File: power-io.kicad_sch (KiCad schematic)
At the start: 30 parts, among them J1 USB4105-GF-A, J2 J2 GPIO / 2.00mm, J3 J3 GPIO / 2.00mm, SW1 RESET, SW2 BOOT, U2 AP2112K-3.3, U4 SN74LV1T125

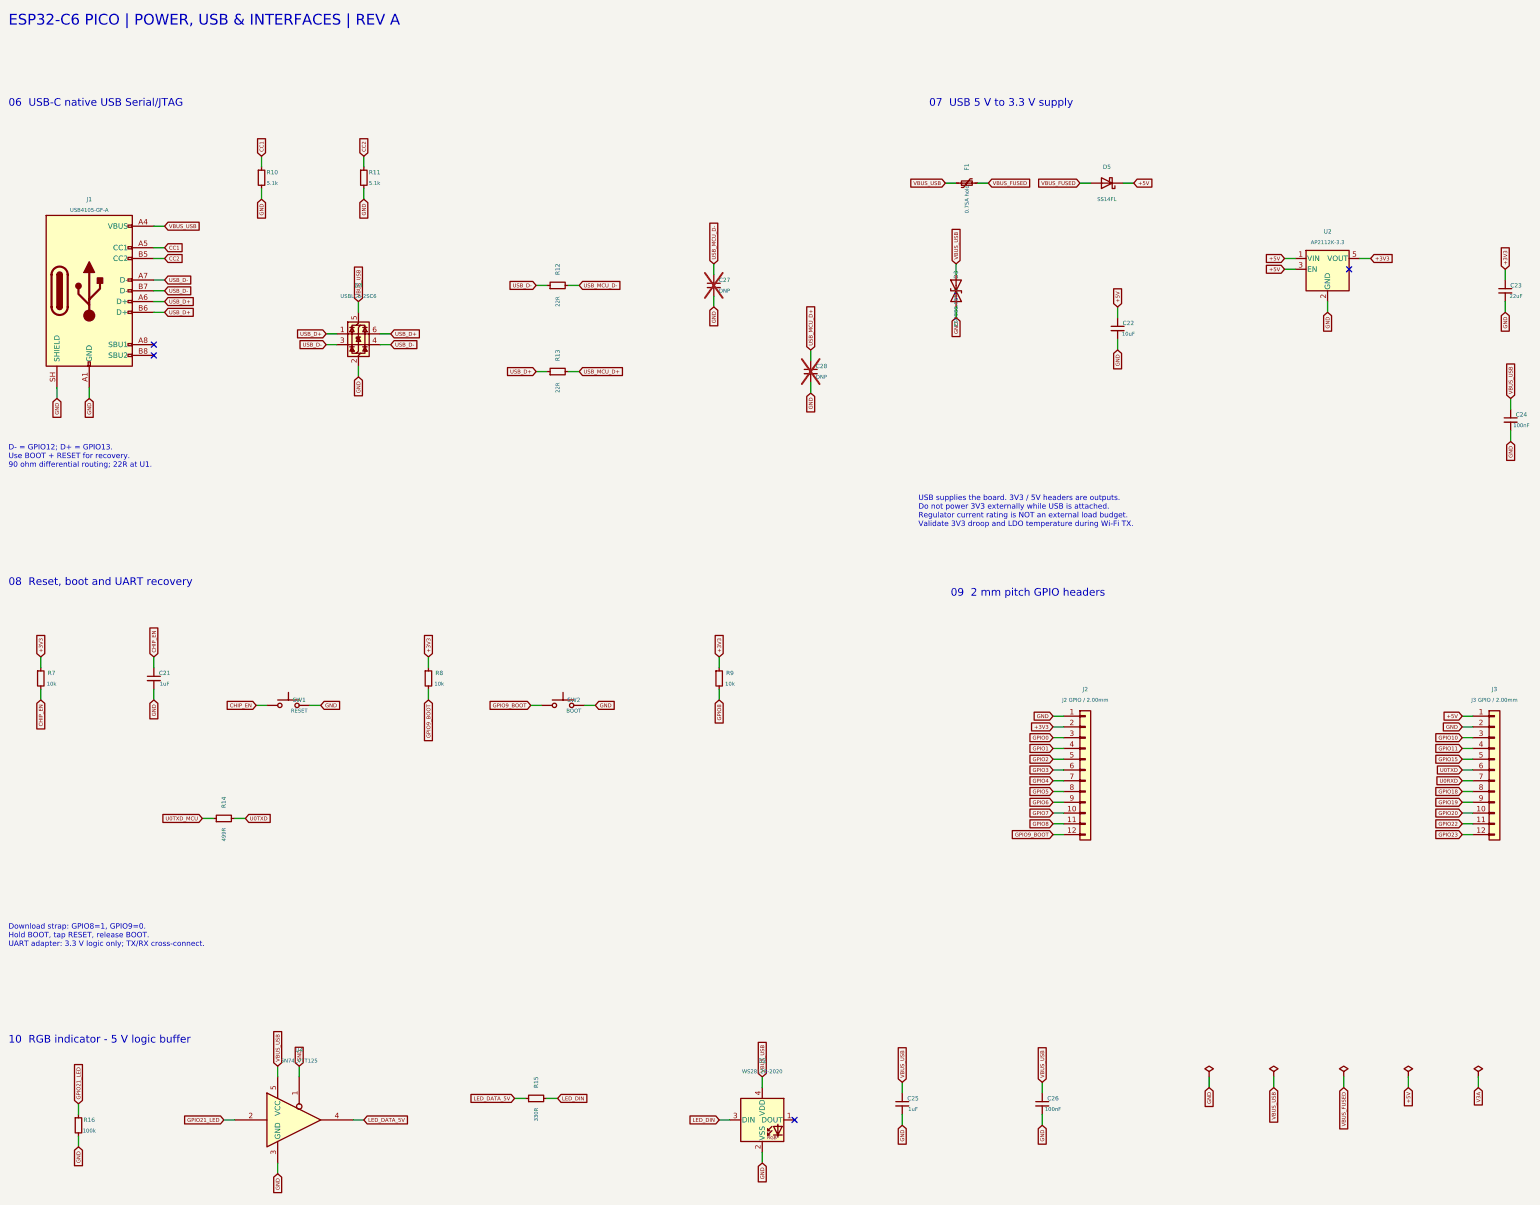
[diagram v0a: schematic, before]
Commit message: Refine ESP32-C6 Pico layout and project handoff
Update the 20.5 x 32 mm layout, antenna and crystal placement, USB routing, via clearances, and silkscreen logos. Keep RF passives at 0201 and use 0402 for all other resistors and capacitors. Draw ESP32-C6 peripherals directly from U1 pins.

Refresh BOM, placement files, previews, validation reports, and project guidance. Exclude KiCad backup folders, autosaves, and local state on Windows and Linux.

Validation: ERC, DRC, and unconnected counts are zero; all 45 QA checks passed. Verify final file hashes and backup exclusions before commit.
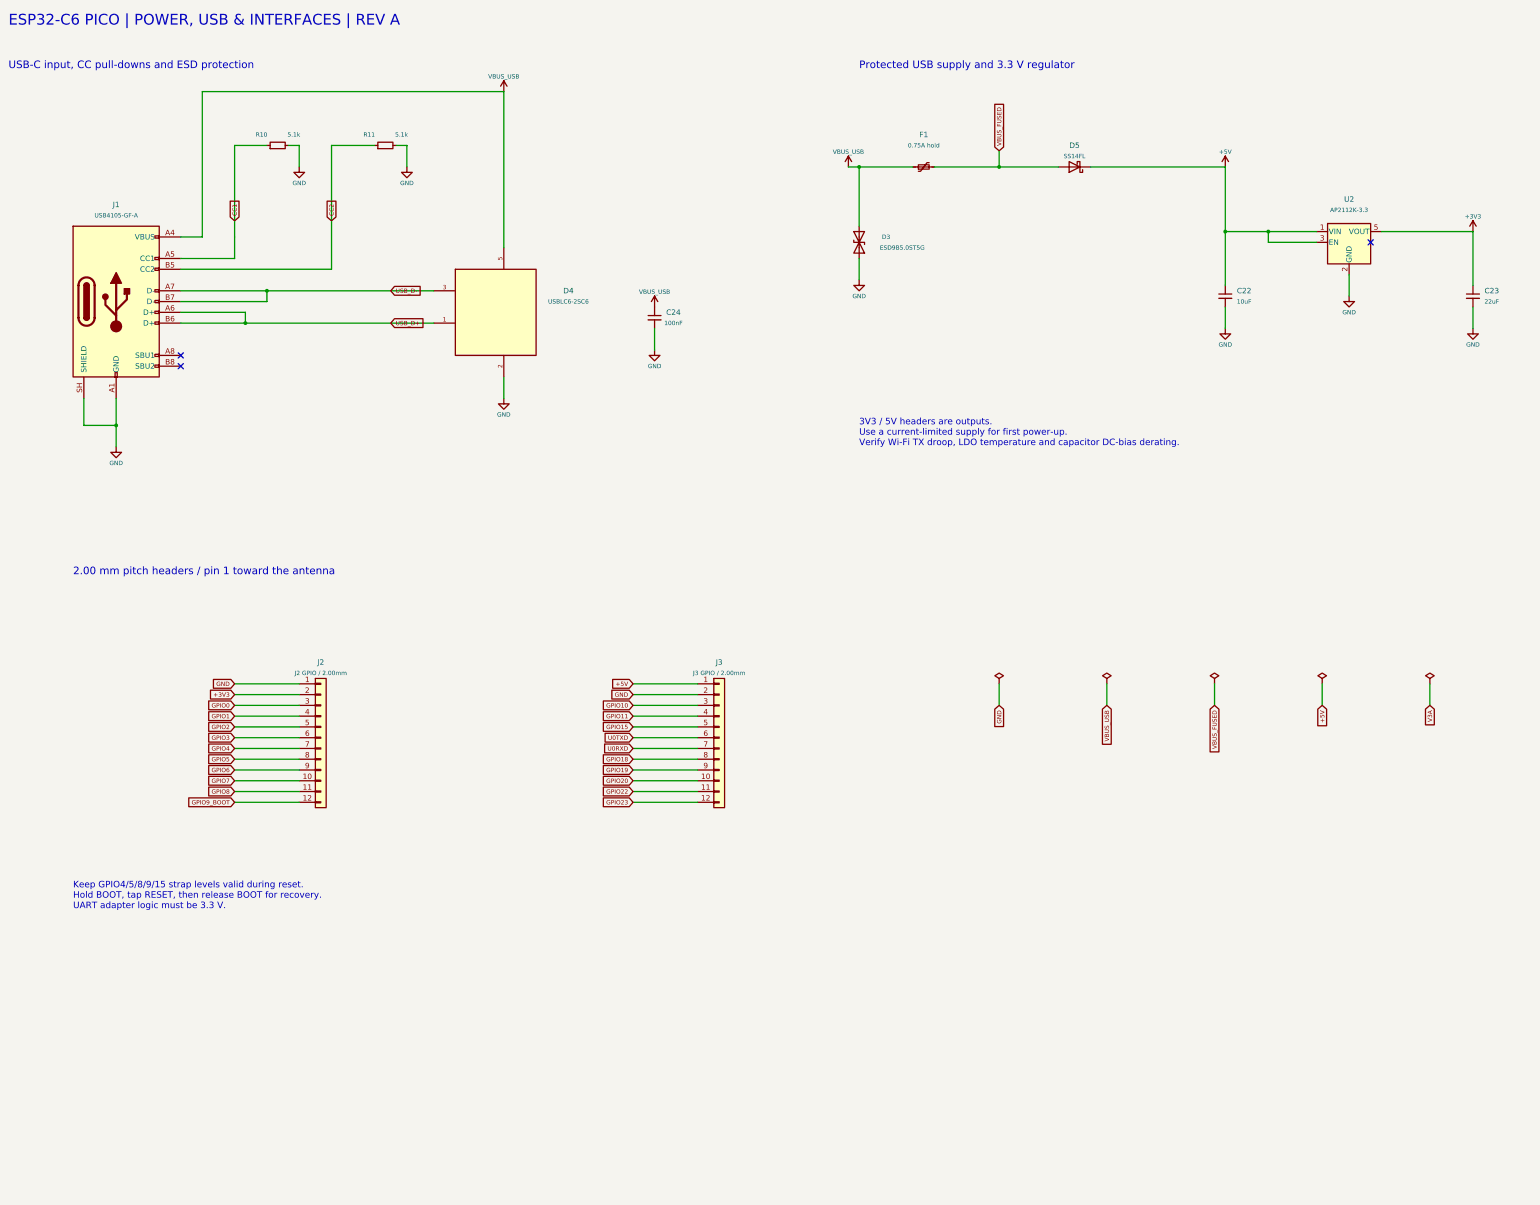
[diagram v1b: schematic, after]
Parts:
- removed C21, C25: 1uF, Capacitor_SMD:C_0402_1005Metric, symbol Pico_Design:Device__C_Small
- removed C26: 100nF, Capacitor_SMD:C_0402_1005Metric, symbol Pico_Design:Device__C_Small
- removed C27, C28: DNP, Capacitor_SMD:C_0402_1005Metric, symbol Pico_Design:Device__C_Small
- removed D2: WS2812B-2020, Pico:WS2812B_2020_Compact, symbol Pico_Design:LED__WS2812B-2020
- removed R12, R13: 22R, Resistor_SMD:R_0402_1005Metric, symbol Pico_Design:Device__R_Small
- removed R14: 499R, Resistor_SMD:R_0402_1005Metric, symbol Pico_Design:Device__R_Small
- removed R15: 330R, Resistor_SMD:R_0402_1005Metric, symbol Pico_Design:Device__R_Small
- removed R16: 100k, Resistor_SMD:R_0402_1005Metric, symbol Pico_Design:Device__R_Small
- removed R7, R8, R9: 10k, Resistor_SMD:R_0402_1005Metric, symbol Pico_Design:Device__R_Small
- removed SW1: RESET, Button_Switch_SMD:SW_Push_1P1T_NO_CK_KMR2, symbol Pico_Design:Switch__SW_Push
- removed SW2: BOOT, Button_Switch_SMD:SW_Push_1P1T_NO_CK_KMR2, symbol Pico_Design:Switch__SW_Push
- removed U4: SN74LV1T125, Package_TO_SOT_SMD:SOT-23-5, symbol Pico_Design:Pico_Custom__SN74LV1T125
- C22: footprint Capacitor_SMD:C_0603_1608Metric -> Capacitor_SMD:C_0402_1005Metric; AssemblyNote 10 V X7R; regulator input -> Regulator input; 0402, 10 V minimum; X5R reference; verify 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
- C23: footprint Capacitor_SMD:C_0603_1608Metric -> Capacitor_SMD:C_0402_1005Metric; AssemblyNote 10 V X5R/X7R; verify DC-bias effective capacitance -> Regulator output; 0402, 22 uF nominal, 10 V minimum; X5R re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
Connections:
- no-connect marks 4 -> 3
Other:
- note added: "2.00 mm pitch headers / pin 1 toward the antenna"
- note added: "3V3 / 5V headers are outputs. Use a current-limited supply for first power-up. Verify Wi-Fi TX droop, LDO temperature and capacitor DC-bias derating."
- note added: "Keep GPIO4/5/8/9/15 strap levels valid during reset. Hold BOOT, tap RESET, then release BOOT for recovery. UART adapter logic must be 3.3 V."
- note added: "Protected USB supply and 3.3 V regulator"
- note added: "USB-C input, CC pull-downs and ESD protection"
- note removed: "06 USB-C native USB Serial/JTAG"
- note removed: "07 USB 5 V to 3.3 V supply"
- note removed: "08 Reset, boot and UART recovery"
- note removed: "09 2 mm pitch GPIO headers"
- note removed: "10 RGB indicator - 5 V logic buffer"
- note removed: "D- = GPIO12; D+ = GPIO13. Use BOOT + RESET for recovery. 90 ohm differential routing; 22R at U1."
- note removed: "Download strap: GPIO8=1, GPIO9=0. Hold BOOT, tap RESET, release BOOT. UART adapter: 3.3 V logic only; TX/RX cross-connect."
- note removed: "USB supplies the board. 3V3 / 5V headers are outputs. Do not power 3V3 externally while USB is attached. Regulator current rating is NOT an external load budget. Validate 3V3 droop and LDO temperature during Wi-Fi TX."
- moved on the sheet: C22, C23, C24, D3, D5, F1, J1, J2, J3, R10, R11, U2
